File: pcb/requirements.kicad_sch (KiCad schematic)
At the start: 0 parts

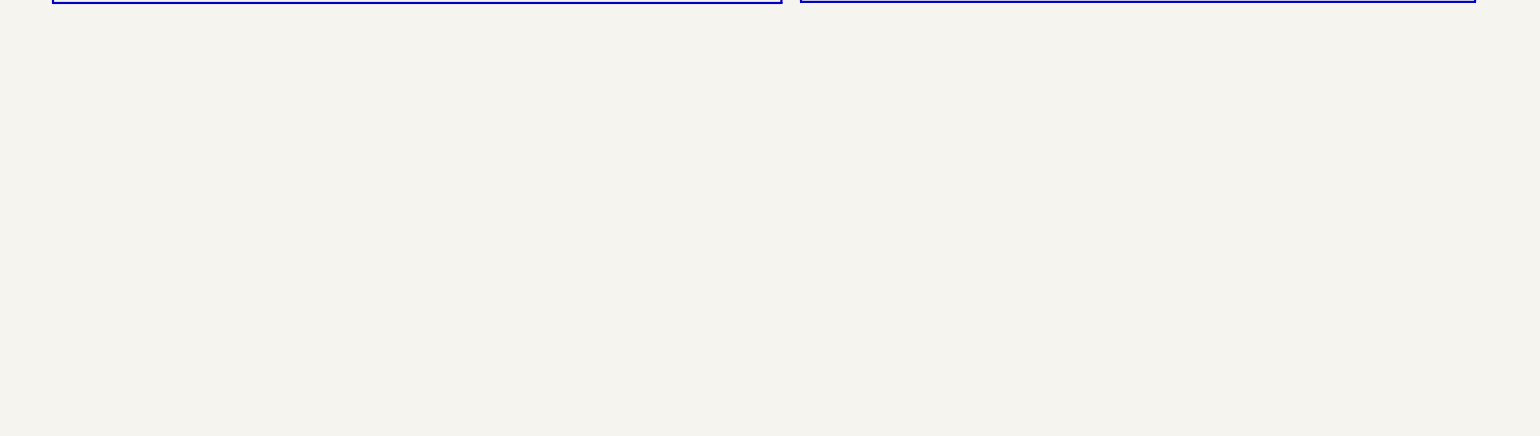
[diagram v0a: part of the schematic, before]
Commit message: Reworked based on new standards
Decreased to 3 servo ports
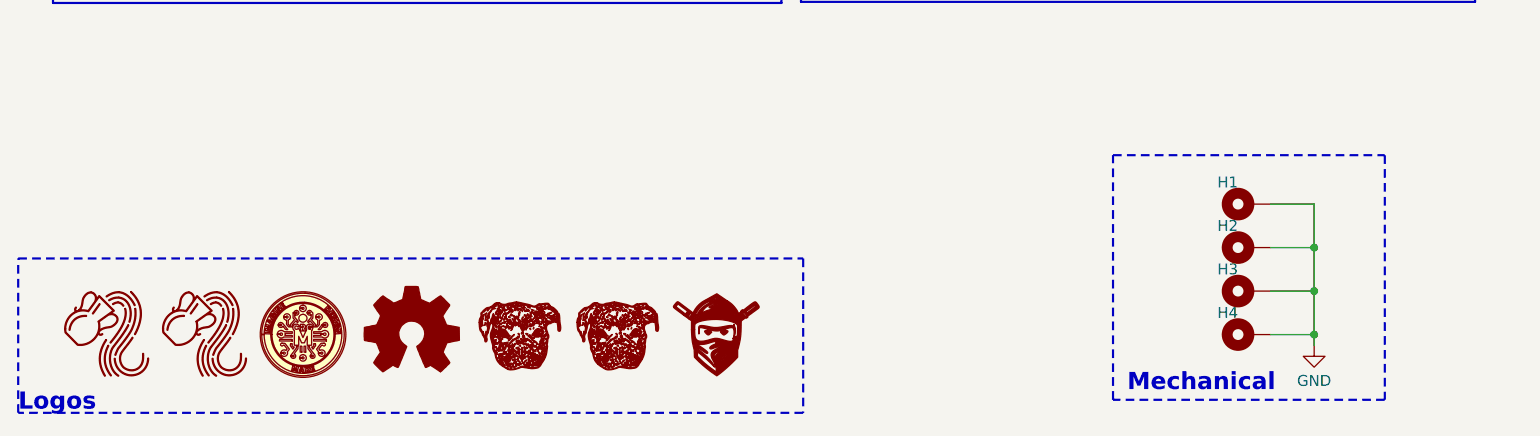
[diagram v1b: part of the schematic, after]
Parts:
- added H1, H2, H3, H4: MountingHole, CRGM Mechanical:MountingHole_3.2mm_M3_Pad_Via, symbol CRGM Mechanical:MountingHole_Pad
- added LOGO1, LOGO2: ~, CRGM Logos:Aquarius Logo 8mm, symbol CRGM Logos:Aquarius Logo
- added LOGO3: ~, CRGM Logos:CRGM Logo 7mm, symbol CRGM Logos:CRGM Logo
- added LOGO4, LOGO5: ~, CRGM Logos:Roxy 8mm, symbol CRGM Logos:Roxy Logo
- added LOGO6: Logo_Open_Hardware_Small, Symbol:OSHW-Logo_5.7x6mm_SilkScreen, symbol Graphic:Logo_Open_Hardware_Small
- added LOGO7: ~, CRGM Logos:FNWW Face 5mm, symbol CRGM Logos:FNWW Face
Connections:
- new net GND: H1.1, H2.1, H3.1, H4.1
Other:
- note added: "Logos"
- note added: "Mechanical"

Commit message: Added status leds
forced to reroute entire board
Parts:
- LOGO1, LOGO2: footprint CRGM Logos:Aquarius Logo 8mm -> CRGM Logos:Aquarius Logo 5mm
- LOGO4, LOGO5: footprint CRGM Logos:Roxy 8mm -> CRGM Logos:Roxy 6.5mm
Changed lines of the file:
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@@
 		)
 	)
-	(text_box "Interfaces:\n* 2 - Power\n* 2 - QWICC\n* 1 - Serial\n* 4 - Servo Out\n\nOUTPUT:\n* 4 Servo Status LEDs\n* 1 5V Power\n* 1 3.3V Power"
+	(text_box "Interfaces:\n* 2 - Power\n* 2 - QWICC\n* 1 - Serial\n* 3 - Servo Out\n\nOUTPUT:\n* 1 5V Power\n* 1 3.3V Power"
 		(exclude_from_sim yes)
 		(at 161.29 32.385 0)
@@
 			)
 		)
-		(property "Footprint" "CRGM Logos:Aquarius Logo 8mm"
+		(property "Footprint" "CRGM Logos:Aquarius Logo 5mm"
 			(at 38.354 189.738 0)
 			(effects
@@
 			)
 		)
-		(property "Footprint" "CRGM Logos:Roxy 8mm"
+		(property "Footprint" "CRGM Logos:Roxy 6.5mm"
 			(at 85.09 194.818 0)
 			(effects
@@
 			)
 		)
-		(property "Footprint" "CRGM Logos:Aquarius Logo 8mm"
+		(property "Footprint" "CRGM Logos:Aquarius Logo 5mm"
 			(at 26.924 189.738 0)
 			(effects
@@
 			)
 		)
-		(property "Footprint" "CRGM Logos:Roxy 8mm"
+		(property "Footprint" "CRGM Logos:Roxy 6.5mm"
 			(at 73.66 194.818 0)
 			(effects

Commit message: Added servo power and filtering
Added connection for servo power
Added solder jumper for servo power to 5V
Added caps to servo power
Added bulk decoupling caps
Added TVS to various inputs
Updated renders
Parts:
- LOGO5: renamed from LOGO4; footprint CRGM Logos:Roxy 6.5mm -> CRGM Logos:Roxy 5mm
- LOGO6: renamed from LOGO5; footprint CRGM Logos:Roxy 6.5mm -> CRGM Logos:Roxy 5mm
- renumbered LOGO6 to LOGO4
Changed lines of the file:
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@@
 		)
 	)
-	(text_box "BASIC\n\n* ATTiny1616 Processor\n* Adafruit Seesaw Protocol\n* Four Servo Ports\n* Power In/Out Ports\n* Optional Pull Ups for I2C\n* I2C Address Selection (2-bits)"
+	(text_box "BASIC\n\n* ATTiny1616 Processor\n* Adafruit Seesaw Protocol\n* Three Servo Ports\n* Power In/Out Ports\n* Optional Pull Ups for I2C\n* I2C Address Selection (2-bits)\n* Servo power connector\n* Servo status indicators"
 		(exclude_from_sim yes)
 		(at 19.05 32.385 0)
@@
 		)
 	)
-	(text_box "Interfaces:\n* 2 - Power\n* 2 - QWICC\n* 1 - Serial\n* 3 - Servo Out\n\nOUTPUT:\n* 1 5V Power\n* 1 3.3V Power"
+	(text_box "Interfaces:\n* 2 - QWICC\n* 2 - Aquarius Power\n* 1 - Servo Power Input\n* 1 - Serial\n* 3 - Servo Out\n\nOUTPUT:\n* 3 Servo Out\n"
 		(exclude_from_sim yes)
 		(at 161.29 32.385 0)
@@
 		(dnp no)
 		(fields_autoplaced yes)
-		(property "Reference" "LOGO6"
+		(property "Reference" "LOGO4"
 			(at 60.96 179.705 0)
 			(effects
@@
 			(project "servo-module"
 				(path "/445c1fff-2e1a-48b1-a91f-a137832edebf/5454c337-e679-4d27-a394-0abf4144d85b"
-					(reference "LOGO6")
+					(reference "LOGO4")
 					(unit 1)
 				)
@@
 		(on_board yes)
 		(dnp no)
-		(property "Reference" "LOGO5"
+		(property "Reference" "LOGO6"
 			(at 85.09 193.04 0)
 			(effects
@@
 			)
 		)
-		(property "Footprint" "CRGM Logos:Roxy 6.5mm"
+		(property "Footprint" "CRGM Logos:Roxy 5mm"
 			(at 85.09 194.818 0)
 			(effects
@@
 			(project "servo-module"
 				(path "/445c1fff-2e1a-48b1-a91f-a137832edebf/5454c337-e679-4d27-a394-0abf4144d85b"
-					(reference "LOGO5")
+					(reference "LOGO6")
 					(unit 1)
 				)
@@
 		(on_board yes)
 		(dnp no)
-		(property "Reference" "LOGO4"
+		(property "Reference" "LOGO5"
 			(at 73.66 193.04 0)
 			(effects
@@
 			)
 		)
-		(property "Footprint" "CRGM Logos:Roxy 6.5mm"
+		(property "Footprint" "CRGM Logos:Roxy 5mm"
 			(at 73.66 194.818 0)
 			(effects
@@
 			(project "servo-module"
 				(path "/445c1fff-2e1a-48b1-a91f-a137832edebf/5454c337-e679-4d27-a394-0abf4144d85b"
-					(reference "LOGO4")
+					(reference "LOGO5")
 					(unit 1)
 				)

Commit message: Finished routing
Updated renders
Added 4th LED
Fixed LED wiring
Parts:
- removed LOGO7: ~, CRGM Logos:FNWW Face 5mm, symbol CRGM Logos:FNWW Face
- LOGO6: footprint CRGM Logos:Roxy 5mm -> CRGM Logos:Roxy 6.5mm
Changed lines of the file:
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@@
-	)
-	(symbol
-		(lib_id "CRGM Logos:FNWW Face")
-		(at 96.52 186.69 0)
-		(unit 1)
-		(exclude_from_sim no)
-		(in_bom no)
-		(on_board yes)
-		(dnp no)
-		(property "Reference" "LOGO7"
-			(at 96.52 193.548 0)
-			(effects
-				(font
-					(size 1.27 1.27)
-				)
-				(hide yes)
-			)
-		)
-		(property "Value" "~"
-			(at 93.98 181.864 0)
-			(effects
-				(font
-					(size 1.27 1.27)
-				)
-				(hide yes)
-			)
-		)
-		(property "Footprint" "CRGM Logos:FNWW Face 5mm"
-			(at 96.52 195.834 0)
-			(effects
-				(font
-					(size 1.27 1.27)
-				)
-				(hide yes)
-			)
-		)
-		(property "Datasheet" ""
-			(at 93.98 181.864 0)
-			(effects
-				(font
-					(size 1.27 1.27)
-				)
-				(hide yes)
-			)
-		)
-		(property "Description" ""
-			(at 93.98 181.864 0)
-			(effects
-				(font
-					(size 1.27 1.27)
-				)
-				(hide yes)
-			)
-		)
-		(property "LCSC" ""
-			(at 96.52 186.69 0)
-			(effects
-				(font
-					(size 1.27 1.27)
-				)
-				(hide yes)
-			)
-		)
-		(property "Digikey" ""
-			(at 96.52 186.69 0)
-			(effects
-				(font
-					(size 1.27 1.27)
-				)
-				(hide yes)
-			)
-		)
-		(property "Mouser" ""
-			(at 96.52 186.69 0)
-			(effects
-				(font
-					(size 1.27 1.27)
-				)
-				(hide yes)
-			)
-		)
-		(instances
-			(project ""
-				(path "/445c1fff-2e1a-48b1-a91f-a137832edebf/5454c337-e679-4d27-a394-0abf4144d85b"
-					(reference "LOGO7")
-					(unit 1)
-				)
-			)
-		)
 	)
 	(symbol
@@
 			)
 		)
-		(property "Footprint" "CRGM Logos:Roxy 5mm"
+		(property "Footprint" "CRGM Logos:Roxy 6.5mm"
 			(at 85.09 194.818 0)
 			(effects

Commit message: Redesign with SMT32
Complete redesign using SMT32 instead of ATTINY.
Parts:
- LOGO2: footprint CRGM Logos:Aquarius Logo 5mm -> CRGM Logos:Aquarius Logo 3.5mm
- LOGO5: footprint CRGM Logos:Roxy 5mm -> CRGM Logos:Roxy 3.5mm
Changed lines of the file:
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@@
 		)
 	)
-	(text_box "BASIC\n\n* ATTiny1616 Processor\n* Adafruit Seesaw Protocol\n* Three Servo Ports\n* Power In/Out Ports\n* Optional Pull Ups for I2C\n* I2C Address Selection (2-bits)\n* Servo power connector\n* Servo status indicators"
+	(text_box "BASIC\n\n* STM3C0 Processor\n* 8MHz Crystal\n* Adafruit Seesaw Protocol\n* Four Servo Ports\n* Power In/Out Ports\n* Optional Pull Ups for I2C\n* I2C Address Selection (2-bits)\n* Servo power connector\n* Servo status indicators"
 		(exclude_from_sim yes)
 		(at 19.05 32.385 0)
@@
 		)
 	)
-	(text_box "Interfaces:\n* 2 - QWICC\n* 2 - Aquarius Power\n* 1 - Servo Power Input\n* 1 - Serial\n* 3 - Servo Out\n\nOUTPUT:\n* 3 Servo Out\n"
+	(text_box "Interfaces:\n* 2 - QWICC\n* 2 - Aquarius Power\n* 1 - Servo Power Input\n* 1 - Serial\n* 1 - Prg/Debug Port\n\nOUTPUT:\n* 4 - Servo Out\n\n"
 		(exclude_from_sim yes)
 		(at 161.29 32.385 0)
@@
 			)
 		)
-		(property "Footprint" "CRGM Logos:Aquarius Logo 5mm"
+		(property "Footprint" "CRGM Logos:Aquarius Logo 3.5mm"
 			(at 38.354 189.738 0)
 			(effects
@@
 			)
 		)
-		(property "Footprint" "CRGM Logos:Roxy 5mm"
+		(property "Footprint" "CRGM Logos:Roxy 3.5mm"
 			(at 73.66 194.818 0)
 			(effects

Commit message: Fixed models; adjusted layout
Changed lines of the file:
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@@
 		)
 	)
-	(text_box "BASIC\n\n* STM3C0 Processor\n* 8MHz Crystal\n* Adafruit Seesaw Protocol\n* Four Servo Ports\n* Power In/Out Ports\n* Optional Pull Ups for I2C\n* I2C Address Selection (2-bits)\n* Servo power connector\n* Servo status indicators"
+	(text_box "BASIC\n\n* STM3C0 Processor\n* 48MHz Crystal\n* Adafruit Seesaw Protocol\n* Four Servo Ports\n* Power In/Out Ports\n* Optional Pull Ups for I2C\n* I2C Address Selection (2-bits)\n* Servo Power Connector\n* Servo Power Indicator\n* Servo Status Indicators\n"
 		(exclude_from_sim yes)
 		(at 19.05 32.385 0)

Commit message: Moved servo power connector to center
Updated silkscreen
Updated renders
Increased size of Roxy ❤️
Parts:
- LOGO5: footprint CRGM Logos:Roxy 3.5mm -> CRGM Logos:Roxy 5mm
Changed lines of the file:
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@@
 			)
 		)
-		(property "Footprint" "CRGM Logos:Roxy 3.5mm"
+		(property "Footprint" "CRGM Logos:Roxy 5mm"
 			(at 73.66 194.818 0)
 			(effects
